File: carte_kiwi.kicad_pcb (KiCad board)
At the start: 2 copper layers, 50 x 50 mm, 35 parts, among them IC1 MCP2562, P1 CONN_01X05, P2 CONN_01X03, P3 CONN_01X05, P4 CONN_01X03, P5 Serial Wire, P6 CAN_conn, P7 CONN_01X03, P8 CONN_01X03, P9 CAN_conn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

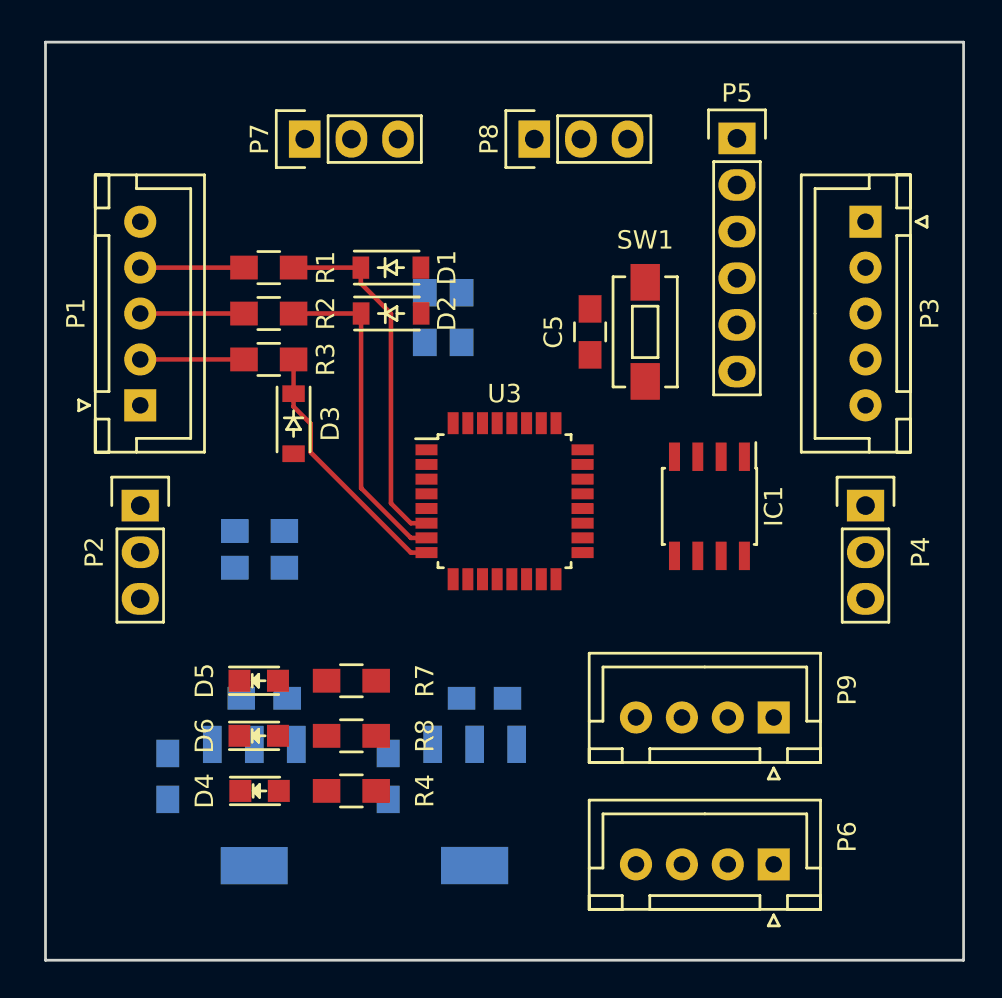
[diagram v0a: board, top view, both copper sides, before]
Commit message: ajoute capa découplage
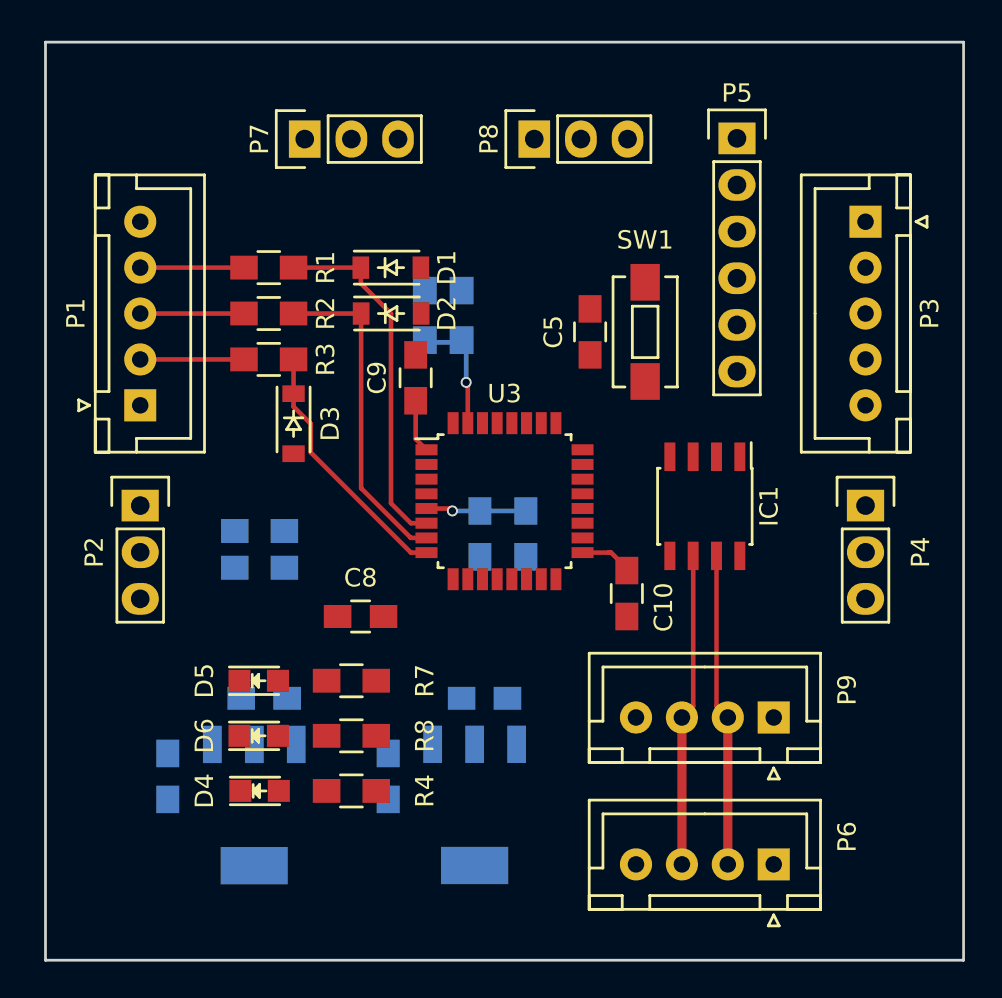
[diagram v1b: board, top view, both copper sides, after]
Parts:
- added C10: 100nF, Capacitors_SMD:C_0805_HandSoldering, F.Cu at (157.0, 115.2)
- added C6: 10nF, Capacitors_SMD:C_0805_HandSoldering, B.Cu at (149.0, 112.0)
- added C7: 1uF, Capacitors_SMD:C_0805_HandSoldering, B.Cu at (151.5, 112.0)
- added C8: 4.7uF, Capacitors_SMD:C_0805_HandSoldering, F.Cu at (142.5, 116.5)
- added C9: 100nF, Capacitors_SMD:C_0805_HandSoldering, F.Cu at (145.5, 103.5)
- moved R10 2.00 mm to (146.0, 100.1), turned to 90 degrees
- moved R9 2.00 mm to (148.0, 100.1), turned to 270 degrees
- moved IC1 0.25 mm to (161.2, 110.5)
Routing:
- net CAN_L: track 0.00 -> 17.1 mm
- net CAN_H: track 0.00 -> 17.1 mm
- net +3V3: track 0.00 -> 11.3 mm, vias 0 -> 1
- net BOOT0: track 0.00 -> 6.54 mm, vias 0 -> 1
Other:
- net class Signal added: clearance 0.2, trace_width 0.25, via_dia 0.6, via_drill 0.4

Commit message: correction inversion SCL et SDA + évite renomage systématique des nets GND en NC
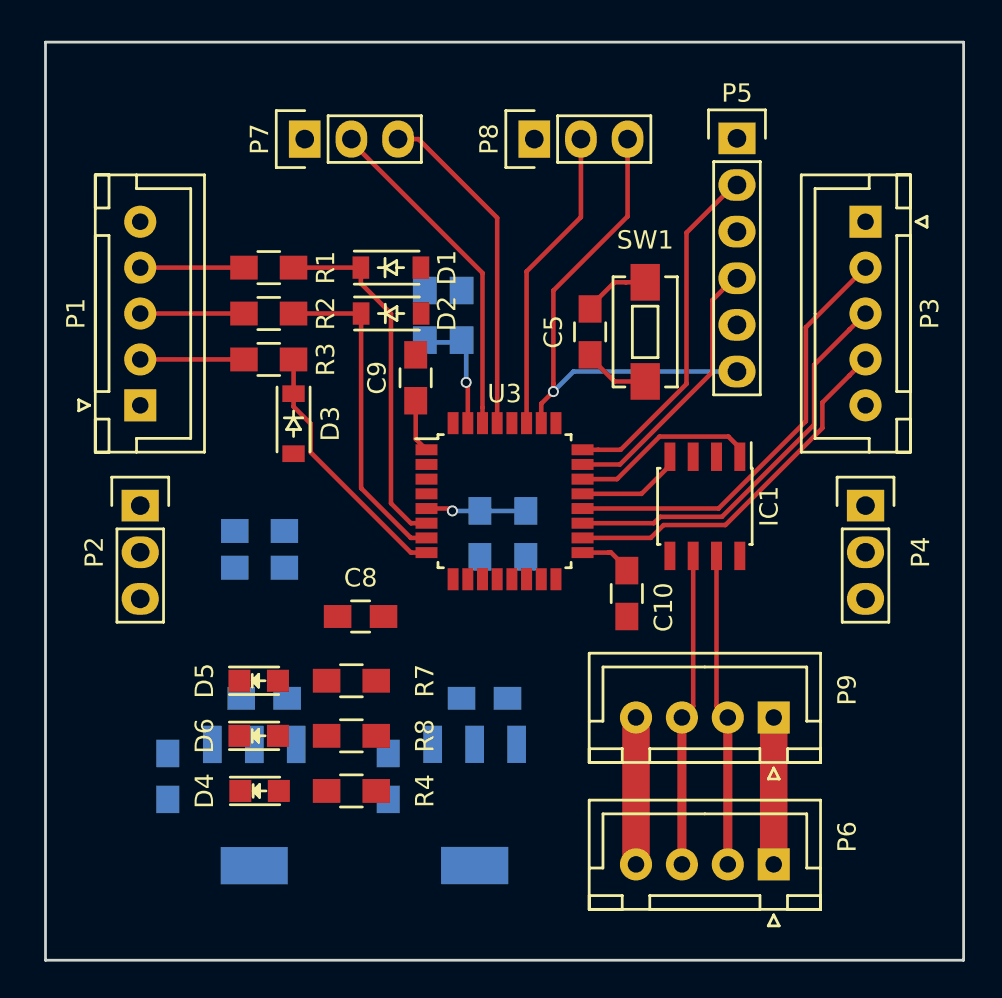
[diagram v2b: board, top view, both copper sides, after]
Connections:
- C1 pad 2: NC -> NC/GND
- C10 pad 2: NC -> NC/GND
- C2 pad 2: NC -> NC/GND
- C3 pad 2: NC -> NC/GND
- C4 pad 2: NC -> NC/GND
- C5 pad 2: NC -> NC/GND
- C6 pad 2: NC -> NC/GND
- C7 pad 2: NC -> NC/GND
- C8 pad 2: NC -> NC/GND
- C9 pad 2: NC -> NC/GND
- D1 pad 2: NC -> NC/GND
- D2 pad 2: NC -> NC/GND
- D3 pad 2: NC -> NC/GND
- D4 pad 1: NC -> NC/GND
- D5 pad 1: NC -> NC/GND
- D6 pad 1: NC -> NC/GND
- IC1 pad 2: NC -> NC/GND
- IC1 pad 8: NC -> NC/GND
- P1 pad 1: NC -> NC/GND
- P2 pad 1: NC -> NC/GND
- P3 pad 1: NC -> NC/GND
- P4 pad 1: NC -> NC/GND
- P5 pad 3: NC -> NC/GND
- P6 pad 4: NC -> NC/GND
- P7 pad 1: NC -> NC/GND
- P7 pad 2: (no net) -> USART1_RX/SDA
- P7 pad 3: (no net) -> USART1_TX/SCL
- P8 pad 1: NC -> NC/GND
- P9 pad 4: NC -> NC/GND
- R10 pad 2: NC -> NC/GND
- SW1 pad 2: NC -> NC/GND
- U1 pad 1: NC -> NC/GND
- U2 pad 1: NC -> NC/GND
- U3 pad 16: NC -> NC/GND
- U3 pad 29: (no net) -> USART1_TX/SCL
- U3 pad 30: (no net) -> USART1_RX/SDA
- U3 pad 32: NC -> NC/GND
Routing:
- net USART2_TX/SWO: track 0.00 -> 27.9 mm, vias 0 -> 1
- net TIM1|Hall3: track 0.00 -> 23.8 mm
- net TIM1|ENCB/Hall2: track 0.00 -> 22.0 mm
- net TIM1|ENCA/Hall1: track 0.00 -> 20.2 mm
- net SWCLK: track 0.00 -> 19.2 mm
- net USART1_RX/SDA: track 0.00 -> 18.4 mm
- net USART1_TX/SCL: track 0.00 -> 18.4 mm
- net USART2_RX: track 0.00 -> 16.7 mm
- net SWDIO: track 0.00 -> 14.9 mm
- net NC/GND: track 0.00 -> 11.7 mm
- net CAN_TX: track 0.00 -> 10.3 mm
- net +9V: track 0.00 -> 8.00 mm
- net CAN_RX: track 0.00 -> 5.87 mm
- net NRST: track 0.00 -> 3.67 mm

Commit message: routage terminé mais à nettoyer
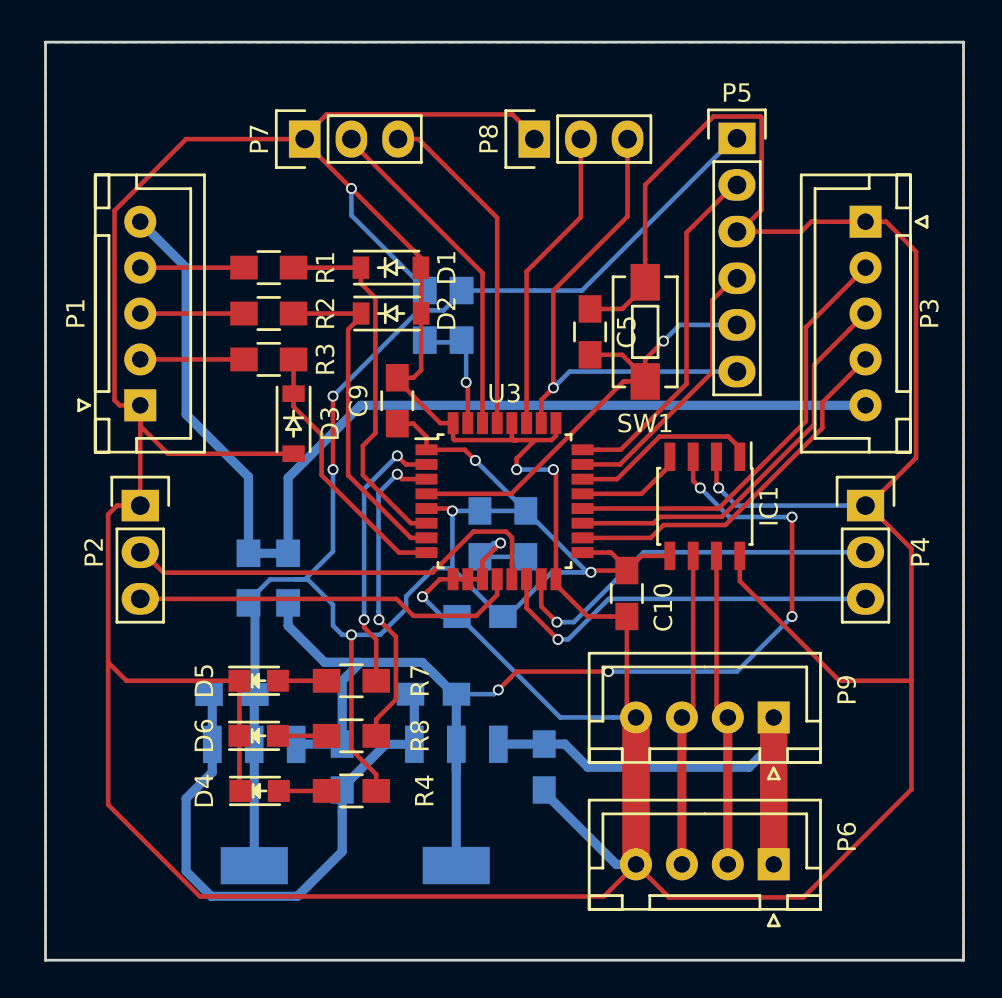
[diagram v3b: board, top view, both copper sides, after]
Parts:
- C8: moved to B.Cu
- moved C8 6.50 mm to (149.0, 116.5), turned to 180 degrees
- moved C4 5.67 mm to (135.5, 120.8), turned to 180 degrees
- moved C3 5.66 mm to (141.5, 124.7), turned to 270 degrees
- moved C2 5.12 mm to (146.5, 120.7), turned to 180 degrees
- moved C1 4.96 mm to (152.5, 124.7), turned to 270 degrees
- moved R5 2.64 mm to (136.4, 114.4), turned to 90 degrees
- moved R6 1.65 mm to (138.6, 114.4), turned to 90 degrees
- moved C9 1.60 mm to (144.5, 104.8)
- moved U1 1.00 mm to (147.7, 126.8)
- turned C5 to 90 degrees
- turned R7 to 180 degrees
- turned R8 to 180 degrees
- turned SW1 to 90 degrees
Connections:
- C1 pad 2: NC/GND -> GND
- C10 pad 2: NC/GND -> GND
- C2 pad 2: NC/GND -> GND
- C3 pad 2: NC/GND -> GND
- C4 pad 2: NC/GND -> GND
- C5 pad 2: NC/GND -> GND
- C6 pad 2: NC/GND -> GND
- C7 pad 2: NC/GND -> GND
- C8 pad 2: NC/GND -> GND
- C9 pad 2: NC/GND -> GND
- D1 pad 2: NC/GND -> GND
- D2 pad 2: NC/GND -> GND
- D3 pad 2: NC/GND -> GND
- D4 pad 1: NC/GND -> GND
- D5 pad 1: NC/GND -> GND
- D6 pad 1: NC/GND -> GND
- IC1 pad 2: NC/GND -> GND
- IC1 pad 8: NC/GND -> GND
- P1 pad 1: NC/GND -> GND
- P2 pad 1: NC/GND -> GND
- P3 pad 1: NC/GND -> GND
- P4 pad 1: NC/GND -> GND
- P5 pad 3: NC/GND -> GND
- P6 pad 4: NC/GND -> GND
- P7 pad 1: NC/GND -> GND
- P8 pad 1: NC/GND -> GND
- P9 pad 4: NC/GND -> GND
- R10 pad 2: NC/GND -> GND
- SW1 pad 2: NC/GND -> GND
- U1 pad 1: NC/GND -> GND
- U2 pad 1: NC/GND -> GND
- U3 pad 10: NC -> GND
- U3 pad 11: NC -> GND
- U3 pad 16: NC/GND -> GND
- U3 pad 2: STATUS_LED -> ACTIVITY_LED
- U3 pad 25: NC -> GND
- U3 pad 28: NC -> GND
- U3 pad 3: ACTIVITY_LED -> STATUS_LED
- U3 pad 32: NC/GND -> GND
- U3 pad 9: NC -> GND
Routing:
- net GND: track 0.00 -> 351.1 mm, vias 0 -> 6
- net +3V3: track 11.3 -> 118.2 mm, vias 1 -> 6
- net +5V: track 0.00 -> 66.2 mm, vias 0 -> 5
- net Sensor_PWR: track 0.00 -> 59.8 mm
- net TIM3|DIR1/PWM2: track 0.00 -> 24.0 mm
- net TIM3|PWM3: track 0.00 -> 21.7 mm, vias 0 -> 1
- net NRST: track 3.67 -> 25.1 mm, vias 0 -> 1
- net TIM3|PWM1: track 0.00 -> 21.1 mm
- net TIM3|DIR2/PWM4: track 0.00 -> 21.1 mm, vias 0 -> 1
- net +9V: track 8.00 -> 25.5 mm
- net STATUS_LED: track 0.00 -> 17.2 mm, vias 0 -> 2
- net ACTIVITY_LED: track 0.00 -> 15.1 mm, vias 0 -> 2
- net NC/GND: track 11.7 -> 0.00 mm
- net Net-(D6-Pad2): track 0.00 -> 2.65 mm
- net Net-(D5-Pad2): track 0.00 -> 2.65 mm
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- added copper zone on B.Cu, net GND
- added copper zone on F.Cu, net GND

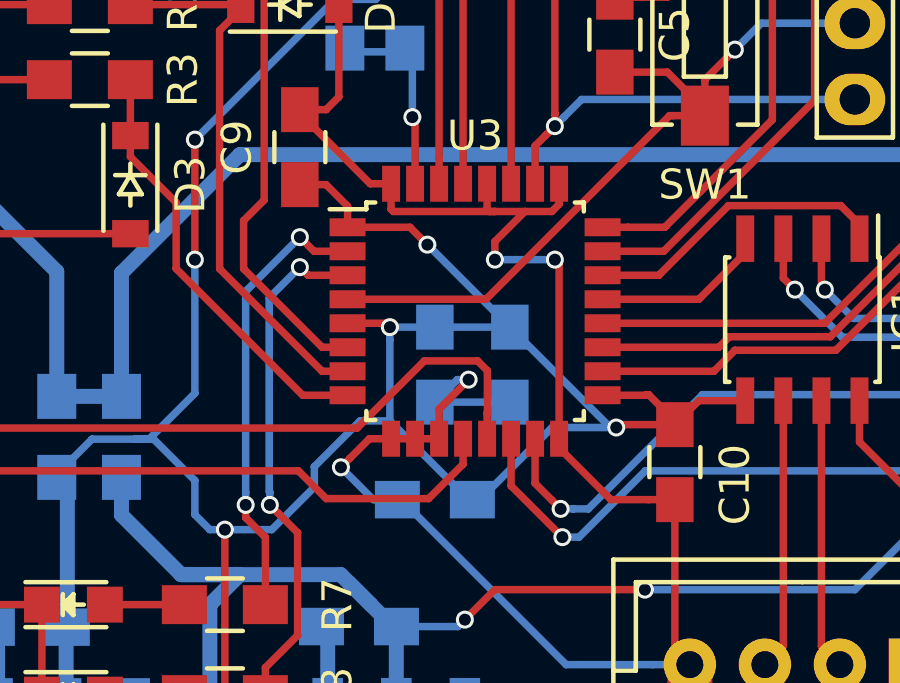
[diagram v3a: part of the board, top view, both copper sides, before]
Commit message: retire les connexions à GND des pins non utilisées
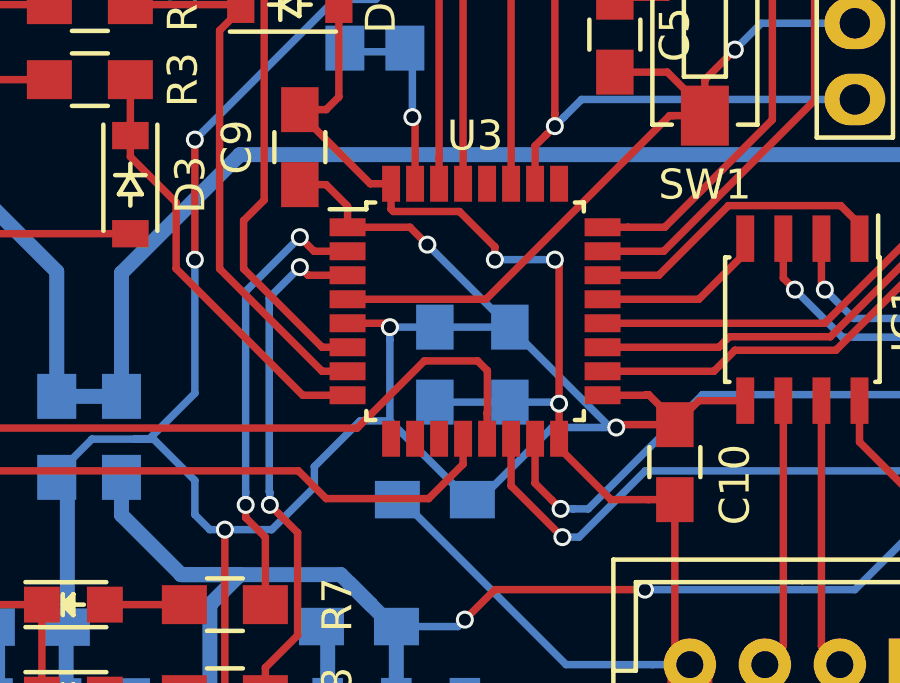
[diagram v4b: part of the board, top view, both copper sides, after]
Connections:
- U3 pad 10: GND -> (no net)
- U3 pad 11: GND -> (no net)
- U3 pad 25: GND -> (no net)
- U3 pad 28: GND -> (no net)
- U3 pad 9: GND -> (no net)
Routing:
- net GND: track 351.1 -> 337.7 mm, vias 6 -> 5
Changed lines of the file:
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@@
 (kicad_pcb (version 4) (host pcbnew 4.0.5)
   (general
-    (links 103)
+    (links 98)
     (no_connects 0)
     (area 125.264999 85.144999 175.415001 135.295001)
     (thickness 1.6)
     (drawings 17)
-    (tracks 417)
+    (tracks 400)
     (zones 0)
     (modules 40)
@@
     (pad 8 smd rect (at -4.25 2.8) (size 1.2 0.6) (layers F.Cu F.Paste F.Mask)
       (net 11 TIM2|Hall3))
-    (pad 9 smd rect (at -2.8 4.25 90) (size 1.2 0.6) (layers F.Cu F.Paste F.Mask)
-      (net 4 GND))
-    (pad 10 smd rect (at -2 4.25 90) (size 1.2 0.6) (layers F.Cu F.Paste F.Mask)
-      (net 4 GND))
-    (pad 11 smd rect (at -1.2 4.25 90) (size 1.2 0.6) (layers F.Cu F.Paste F.Mask)
-      (net 4 GND))
+    (pad 9 smd rect (at -2.8 4.25 90) (size 1.2 0.6) (layers F.Cu F.Paste F.Mask))
+    (pad 10 smd rect (at -2 4.25 90) (size 1.2 0.6) (layers F.Cu F.Paste F.Mask))
+    (pad 11 smd rect (at -1.2 4.25 90) (size 1.2 0.6) (layers F.Cu F.Paste F.Mask))
     (pad 12 smd rect (at -0.4 4.25 90) (size 1.2 0.6) (layers F.Cu F.Paste F.Mask)
       (net 21 TIM3|PWM1))
@@
     (pad 24 smd rect (at 4.25 -2.8) (size 1.2 0.6) (layers F.Cu F.Paste F.Mask)
       (net 18 SWCLK))
-    (pad 25 smd rect (at 2.8 -4.25 90) (size 1.2 0.6) (layers F.Cu F.Paste F.Mask)
-      (net 4 GND))
+    (pad 25 smd rect (at 2.8 -4.25 90) (size 1.2 0.6) (layers F.Cu F.Paste F.Mask))
     (pad 26 smd rect (at 2 -4.25 90) (size 1.2 0.6) (layers F.Cu F.Paste F.Mask)
       (net 20 USART2_TX/SWO))
     (pad 27 smd rect (at 1.2 -4.25 90) (size 1.2 0.6) (layers F.Cu F.Paste F.Mask)
       (net 28 USART2_RX))
-    (pad 28 smd rect (at 0.4 -4.25 90) (size 1.2 0.6) (layers F.Cu F.Paste F.Mask)
-      (net 4 GND))
+    (pad 28 smd rect (at 0.4 -4.25 90) (size 1.2 0.6) (layers F.Cu F.Paste F.Mask))
     (pad 29 smd rect (at -0.4 -4.25 90) (size 1.2 0.6) (layers F.Cu F.Paste F.Mask)
       (net 32 USART1_TX/SCL))
@@
   (segment (start 161.885 121.385) (end 162.5 122) (width 0.25) (layer F.Cu) (net 3))
   (segment (start 162.5 130) (end 162.5 122) (width 0.5) (layer F.Cu) (net 3))
-  (segment (start 151 106.895001) (end 152 106.895001) (width 0.25) (layer F.Cu) (net 4))
-  (segment (start 152 106.895001) (end 152.900001 106.895001) (width 0.25) (layer F.Cu) (net 4))
-  (segment (start 151 108.5) (end 151 107.895001) (width 0.25) (layer F.Cu) (net 4))
-  (segment (start 151 107.895001) (end 152 106.895001) (width 0.25) (layer F.Cu) (net 4))
+  (segment (start 153.14 114.47) (end 153.14 113.3) (width 0.25) (layer F.Cu) (net 4))
+  (segment (start 153.09 113.25) (end 153.14 113.3) (width 0.25) (layer B.Cu) (net 4))
+  (segment (start 153.14 113.3) (end 153.14 108.64) (width 0.25) (layer F.Cu) (net 4))
+  (segment (start 151.5 113.25) (end 153.09 113.25) (width 0.25) (layer B.Cu) (net 4))
+  (via (at 153.14 113.3) (size 0.6) (drill 0.4) (layers F.Cu B.Cu) (net 4))
+  (segment (start 147.54 105.97) (end 147.54 106.82) (width 0.25) (layer F.Cu) (net 4))
+  (segment (start 147.54 106.82) (end 147.615001 106.895001) (width 0.25) (layer F.Cu) (net 4))
+  (segment (start 151 108.5) (end 151 108.075736) (width 0.25) (layer F.Cu) (net 4))
+  (segment (start 151 108.075736) (end 149.819265 106.895001) (width 0.25) (layer F.Cu) (net 4))
+  (segment (start 149.819265 106.895001) (end 147.615001 106.895001) (width 0.25) (layer F.Cu) (net 4))
   (via (at 151 108.5) (size 0.6) (drill 0.4) (layers F.Cu B.Cu) (net 4))
   (segment (start 153 108.5) (end 151 108.5) (width 0.25) (layer B.Cu) (net 4))
-  (segment (start 153.14 114.47) (end 153.14 108.64) (width 0.25) (layer F.Cu) (net 4))
   (via (at 153 108.5) (size 0.6) (drill 0.4) (layers F.Cu B.Cu) (net 4))
   (segment (start 153.14 108.64) (end 153 108.5) (width 0.25) (layer F.Cu) (net 4))
-  (segment (start 149.14 113.485002) (end 150.125002 112.5) (width 0.25) (layer F.Cu) (net 4))
-  (segment (start 149.14 114.47) (end 149.14 113.485002) (width 0.25) (layer F.Cu) (net 4))
-  (segment (start 150.125002 112.5) (end 150 112.5) (width 0.25) (layer B.Cu) (net 4))
-  (segment (start 150.125002 112.5) (end 149.75 112.5) (width 0.25) (layer B.Cu) (net 4))
-  (segment (start 149.75 112.5) (end 149 113.25) (width 0.25) (layer B.Cu) (net 4))
-  (via (at 150.125002 112.5) (size 0.6) (drill 0.4) (layers F.Cu B.Cu) (net 4))
-  (segment (start 147.615001 106.895001) (end 151 106.895001) (width 0.25) (layer F.Cu) (net 4))
-  (segment (start 150.74 105.97) (end 150.74 106.82) (width 0.25) (layer F.Cu) (net 4))
-  (segment (start 150.74 106.82) (end 150.815001 106.895001) (width 0.25) (layer F.Cu) (net 4))
-  (segment (start 150.815001 106.895001) (end 151 106.895001) (width 0.25) (layer F.Cu) (net 4))
-  (segment (start 147.54 105.97) (end 147.54 106.82) (width 0.25) (layer F.Cu) (net 4))
-  (segment (start 147.54 106.82) (end 147.615001 106.895001) (width 0.25) (layer F.Cu) (net 4))
-  (segment (start 152.900001 106.895001) (end 153.14 106.655002) (width 0.25) (layer F.Cu) (net 4))
-  (segment (start 153.14 106.655002) (end 153.14 105.97) (width 0.25) (layer F.Cu) (net 4))
-  (segment (start 147.75 116.5) (end 146.947595 116.5) (width 0.25) (layer B.Cu) (net 4))
-  (segment (start 146.947595 116.5) (end 145.868765 115.42117) (width 0.25) (layer B.Cu) (net 4))
-  (segment (start 146.168764 115.121171) (end 145.868765 115.42117) (width 0.25) (layer F.Cu) (net 4))
-  (segment (start 147.54 114.47) (end 146.819935 114.47) (width 0.25) (layer F.Cu) (net 4))
-  (via (at 145.868765 115.42117) (size 0.6) (drill 0.4) (layers F.Cu B.Cu) (net 4))
-  (segment (start 146.819935 114.47) (end 146.168764 115.121171) (width 0.25) (layer F.Cu) (net 4))
-  (segment (start 149.14 114.47) (end 148.34 114.47) (width 0.25) (layer F.Cu) (net 4))
-  (segment (start 147.54 114.47) (end 148.34 114.47) (width 0.25) (layer F.Cu) (net 4))
   (segment (start 151.5 113.25) (end 149 113.25) (width 0.25) (layer B.Cu) (net 4))
   (segment (start 145.785 96.9774) (end 142 93.1924) (width 0.25) (layer F.Cu) (net 4))
